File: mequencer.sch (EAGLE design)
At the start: 58 parts, among them IC1 NE555D, IC10 LF353D, IC11 NE555D, IC12 NE555D, IC2 4163D, IC3 74HC85D, IC4 4051D, IC5 4051D, IC6 74HCT04D, IC7 4051D, IC8 4051D, IC9 LF353D

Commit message: 55555555555555555
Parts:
- added C3, C4: 1uF, SparkFun-Capacitors:CAP0603-CAP
- added R22: 1k, SparkFun-Resistors:RESISTOR0603
- added R23: TRIMPOT-2, SparkFun-Electromechanical:TRIMPOT-2
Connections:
- new net N$16: IC11.DIS, R22.2
- new net N$17: IC12.DIS, R23.CW
- new net N$18: C3.2, IC11.TRE
- new net N$20: IC11.TRI, IC6C.O
- new net N$21: C4.2, IC12.TRE
- new net N$23: IC11.OUT, IC12.TRI
- net 5V: now also IC11./RES, IC11.VCC+, IC12./RES, IC12.VCC+, R22.1, R23.WIPER
- net CLOCK: now also IC6C.I
- net GND: now also C3.1, C4.1, IC11.GND
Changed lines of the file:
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@@
 <part name="IC11" library="SparkFun-AnalogIC" deviceset="NE555" device="D"/>
 <part name="IC12" library="SparkFun-AnalogIC" deviceset="NE555" device="D"/>
+<part name="R22" library="SparkFun-Resistors" deviceset="RESISTOR" device="0603" value="1k"/>
+<part name="SUPPLY8" library="SparkFun-Aesthetics" deviceset="5V" device=""/>
+<part name="GND11" library="SparkFun-Aesthetics" deviceset="GND" device=""/>
+<part name="C3" library="SparkFun-Capacitors" deviceset="CAP" device="0603-CAP" value="1uF"/>
+<part name="GND12" library="SparkFun-Aesthetics" deviceset="GND" device=""/>
+<part name="C4" library="SparkFun-Capacitors" deviceset="CAP" device="0603-CAP" value="1uF"/>
+<part name="SUPPLY9" library="SparkFun-Aesthetics" deviceset="5V" device=""/>
+<part name="R23" library="SparkFun-Electromechanical" deviceset="TRIMPOT" device="-2"/>
 </parts>
 <sheets>
@@
 <instance part="IC11" gate="G$1" x="40.64" y="17.78"/>
 <instance part="IC12" gate="G$1" x="73.66" y="17.78"/>
+<instance part="R22" gate="G$1" x="25.4" y="17.78"/>
+<instance part="SUPPLY8" gate="G$1" x="22.86" y="30.48"/>
+<instance part="GND11" gate="1" x="22.86" y="2.54"/>
+<instance part="C3" gate="G$1" x="5.08" y="12.7" rot="R180"/>
+<instance part="IC6" gate="C" x="20.32" y="12.7"/>
+<instance part="GND12" gate="1" x="60.96" y="2.54"/>
+<instance part="C4" gate="G$1" x="58.42" y="25.4" rot="R180"/>
+<instance part="SUPPLY9" gate="G$1" x="71.12" y="30.48"/>
+<instance part="R23" gate="R?" x="53.34" y="30.48" rot="R270"/>
 </instances>
 <busses>
@@
 <wire x1="30.48" y1="86.36" x2="33.02" y2="86.36" width="0.1524" layer="91"/>
 </segment>
+<segment>
+<pinref part="SUPPLY8" gate="G$1" pin="5V"/>
+<wire x1="22.86" y1="30.48" x2="50.8" y2="30.48" width="0.1524" layer="91"/>
+<pinref part="R22" gate="G$1" pin="1"/>
+<wire x1="20.32" y1="17.78" x2="20.32" y2="30.48" width="0.1524" layer="91"/>
+<wire x1="20.32" y1="30.48" x2="22.86" y2="30.48" width="0.1524" layer="91"/>
+<junction x="22.86" y="30.48"/>
+<pinref part="IC11" gate="G$1" pin="/RES"/>
+<pinref part="IC11" gate="G$1" pin="VCC+"/>
+<wire x1="50.8" y1="22.86" x2="50.8" y2="25.4" width="0.1524" layer="91"/>
+<wire x1="50.8" y1="25.4" x2="50.8" y2="30.48" width="0.1524" layer="91"/>
+<junction x="50.8" y="25.4"/>
+</segment>
+<segment>
+<pinref part="R23" gate="R?" pin="WIPER"/>
+<pinref part="SUPPLY9" gate="G$1" pin="5V"/>
+<wire x1="58.42" y1="30.48" x2="71.12" y2="30.48" width="0.1524" layer="91"/>
+<pinref part="IC12" gate="G$1" pin="/RES"/>
+<pinref part="IC12" gate="G$1" pin="VCC+"/>
+<wire x1="83.82" y1="22.86" x2="83.82" y2="25.4" width="0.1524" layer="91"/>
+<wire x1="83.82" y1="25.4" x2="83.82" y2="30.48" width="0.1524" layer="91"/>
+<junction x="83.82" y="25.4"/>
+<wire x1="83.82" y1="30.48" x2="71.12" y2="30.48" width="0.1524" layer="91"/>
+<junction x="71.12" y="30.48"/>
+</segment>
 </net>
 <net name="N$1" class="0">
@@
 <wire x1="30.48" y1="63.5" x2="30.48" y2="60.96" width="0.1524" layer="91"/>
 </segment>
+<segment>
+<pinref part="IC11" gate="G$1" pin="GND"/>
+<wire x1="50.8" y1="10.16" x2="50.8" y2="5.08" width="0.1524" layer="91"/>
+<pinref part="GND11" gate="1" pin="GND"/>
+<wire x1="50.8" y1="5.08" x2="22.86" y2="5.08" width="0.1524" layer="91"/>
+<junction x="22.86" y="5.08"/>
+<pinref part="C3" gate="G$1" pin="1"/>
+<wire x1="22.86" y1="5.08" x2="5.08" y2="5.08" width="0.1524" layer="91"/>
+<wire x1="5.08" y1="5.08" x2="5.08" y2="7.62" width="0.1524" layer="91"/>
+</segment>
+<segment>
+<pinref part="C4" gate="G$1" pin="1"/>
+<wire x1="58.42" y1="20.32" x2="58.42" y2="5.08" width="0.1524" layer="91"/>
+<pinref part="GND12" gate="1" pin="GND"/>
+<wire x1="58.42" y1="5.08" x2="60.96" y2="5.08" width="0.1524" layer="91"/>
+</segment>
 </net>
 <net name="N$2" class="0">
@@
 <wire x1="17.78" y1="99.06" x2="2.54" y2="99.06" width="0.1524" layer="91"/>
 <label x="2.54" y="99.06" size="1.778" layer="95"/>
+</segment>
+<segment>
+<pinref part="IC6" gate="C" pin="I"/>
+<wire x1="10.16" y1="12.7" x2="7.62" y2="12.7" width="0.1524" layer="91"/>
+<label x="7.62" y="12.7" size="1.778" layer="95"/>
 </segment>
 </net>
@@
 </segment>
 </net>
+<net name="N$16" class="0">
+<segment>
+<pinref part="IC11" gate="G$1" pin="DIS"/>
+<pinref part="R22" gate="G$1" pin="2"/>
+</segment>
+</net>
+<net name="N$18" class="0">
+<segment>
+<pinref part="IC11" gate="G$1" pin="TRE"/>
+<pinref part="C3" gate="G$1" pin="2"/>
+<wire x1="5.08" y1="15.24" x2="5.08" y2="25.4" width="0.1524" layer="91"/>
+<wire x1="5.08" y1="25.4" x2="30.48" y2="25.4" width="0.1524" layer="91"/>
+</segment>
+</net>
+<net name="N$20" class="0">
+<segment>
+<pinref part="IC6" gate="C" pin="O"/>
+<pinref part="IC11" gate="G$1" pin="TRI"/>
+<wire x1="30.48" y1="12.7" x2="30.48" y2="10.16" width="0.1524" layer="91"/>
+</segment>
+</net>
+<net name="N$17" class="0">
+<segment>
+<pinref part="R23" gate="R?" pin="CW"/>
+<wire x1="53.34" y1="25.4" x2="53.34" y2="17.78" width="0.1524" layer="91"/>
+<pinref part="IC12" gate="G$1" pin="DIS"/>
+<wire x1="53.34" y1="17.78" x2="63.5" y2="17.78" width="0.1524" layer="91"/>
+</segment>
+</net>
+<net name="N$21" class="0">
+<segment>
+<pinref part="C4" gate="G$1" pin="2"/>
+<pinref part="IC12" gate="G$1" pin="TRE"/>
+<wire x1="58.42" y1="27.94" x2="63.5" y2="27.94" width="0.1524" layer="91"/>
+<wire x1="63.5" y1="27.94" x2="63.5" y2="25.4" width="0.1524" layer="91"/>
+</segment>
+</net>
+<net name="N$23" class="0">
+<segment>
+<pinref part="IC11" gate="G$1" pin="OUT"/>
+<wire x1="50.8" y1="17.78" x2="50.8" y2="15.24" width="0.1524" layer="91"/>
+<wire x1="50.8" y1="15.24" x2="53.34" y2="15.24" width="0.1524" layer="91"/>
+<wire x1="53.34" y1="15.24" x2="53.34" y2="10.16" width="0.1524" layer="91"/>
+<pinref part="IC12" gate="G$1" pin="TRI"/>
+<wire x1="53.34" y1="10.16" x2="63.5" y2="10.16" width="0.1524" layer="91"/>
+</segment>
+</net>

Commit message: Board1 headers and power and stuff. schematic done?
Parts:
- removed LED1, LED10, LED11, LED12, LED13, LED14, LED15, LED16, LED2, LED3, LED4, LED5, LED6, LED7, LED8, LED9: (no value), SparkFun-LED:LED0603
- removed R2, R23: TRIMPOT-2, SparkFun-Electromechanical:TRIMPOT-2
- removed R3, R4: (no value), SparkFun-Resistors:RESISTOR0603
- removed S1: SWITCH-MOMENTARY-2-SMD-1101NE, SparkFun-Electromechanical:SWITCH-MOMENTARY-2-SMD-1101NE
- added C10, C11, C12, C13, C14, C15, C16, C17, C18, C19, C20, C21, C22, C23, C24, C25, C7, C8, C9: .1uF, SparkFun-Capacitors:CAP0603-CAP
- added C5: 1uF, SparkFun-Capacitors:CAP0603-CAP
- added C6: 10uF, SparkFun-Capacitors:CAP0603-CAP
- added FRAME2: FRAME-LETTER, SparkFun-Aesthetics:FRAME-LETTER
- added JP1: M02LOCK_LONGPADS, SparkFun-Connectors:M02LOCK_LONGPADS
- added JP2, JP3: M20, SparkFun-Connectors:M20
- added R24: 100k, SparkFun-Resistors:RESISTOR0603
- added R25: 4k, SparkFun-Resistors:RESISTOR0603
- added U$5: AUDIO-JACKERTHENVAR, erthenvar:AUDIO-JACKERTHENVAR
- added U$6: LM3480IM4, SparkFun-PowerIC:LM3480IM4
- added U1: 74LVC1G08SE-7, SparkFun-DigitalIC:7408SE
- U$1: value SWITCH-SPST-2TV -> M04X2; device SparkFun-Electromechanical:SWITCH-SPST-2TV -> SparkFun-Connectors:M04X2
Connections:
- removed net N$17: IC12.DIS, R23.CW
- removed net N$3: R1.1, R2.CW, R2.WIPER
- removed net N$4: R2.CCW, R3.1
- removed net N$5: U$1.O, U$2.NORM
- removed net N$6: IC1.OUT, U$1.P
- new net CANNEL3: JP2.4
- new net CLOCK_SPEED: JP2.17, R1.1
- new net CV: IC10A.-IN
- new net N$22: IC10A.OUT, U1.B
- new net N$24: IC10A.+IN, R24.1, R25.2
- new net N$25: U1.A
- new net N$26: U1.Y
- new net N$27: C5.2, JP1.2, U$6.IN
- new net N$29: JP3.19
- new net NOTE_LENGTH: IC12.DIS, JP3.18
- new net PAUSE_IN: IC1.OUT, JP2.18
- new net PAUSE_OUT: JP2.19, U$2.NORM
- net 5V: now also C10.2, C11.2, C13.2, C14.2, C15.2, C16.2, C17.2, C18.2, C19.2, C20.2, C21.2, C22.2, C23.2, C24.2, C25.2, C6.2, C7.2, C8.2, C9.2, JP3.20, R25.1, U$6.OUT, U1.VCC; no longer R23.WIPER, R3.2
- net CHANNEL10: now also JP2.11
- net CHANNEL11: now also JP2.12
- net CHANNEL12: now also JP2.13
- net CHANNEL13: now also JP2.14
- net CHANNEL14: now also JP2.15
- net CHANNEL15: now also JP2.16
- net CHANNEL2: now also JP2.3
- net CHANNEL4: now also JP2.5
- net CHANNEL5: now also JP2.6
- net CHANNEL6: now also JP2.7
- net CHANNEL8: now also JP2.9
- net CHANNEL9: now also JP2.10
- net GND: now also C5.1, C6.1, IC10P.V-, IC3P.GND, IC4P.GND, IC4P.VEE, IC5P.GND, IC5P.VEE, IC6P.GND, IC7P.GND, IC7P.VEE, IC8P.GND, IC8P.VEE, IC9P.V-, JP1.1, JP2.20, R24.2, U$5.RING, U$6.GND, U1.GND; no longer LED1.C, LED10.C, LED11.C, LED12.C, LED13.C, LED14.C, LED15.C, LED16.C, LED2.C, LED3.C, LED4.C, LED5.C, LED6.C, LED7.C, LED8.C, LED9.C, R4.1
- net LED0: no longer LED1.A
- net LED1: now also JP3.2; no longer LED2.A
- net LED10: now also JP3.11; no longer LED11.A
- net LED11: now also JP3.12; no longer LED12.A
- net LED12: now also JP3.13; no longer LED13.A
- net LED13: now also JP3.14; no longer LED14.A
- net LED14: now also JP3.15; no longer LED15.A
- net LED15: now also JP3.16; no longer LED16.A
- net LED2: now also JP3.3; no longer LED3.A
- net LED3: now also JP3.4; no longer LED4.A
- net LED4: now also JP3.5; no longer LED5.A
- net LED5: now also JP3.6; no longer LED6.A
- net LED6: now also JP3.7; no longer LED7.A
- net LED7: now also JP3.8; no longer LED8.A
- net LED8: now also JP3.9; no longer LED9.A
- net LED9: now also JP3.10; no longer LED10.A
- net LOAD: no longer S1.2
- net LOAD0: now also U$1.2
- net LOAD1: now also U$1.4
- net LOAD2: now also U$1.6
- net LOAD3: now also U$1.8
- net N$7: now also C10.1, C11.1, C12.1, C13.1, C14.1, C15.1, C16.1, C17.1, C18.1, C19.1, C20.1, C21.1, C22.1, C23.1, C24.1, C25.1, C7.1, C8.1, C9.1, IC10P.V+, IC2P.VDD, IC3P.VCC, IC4P.VCC, IC5P.VCC, IC6P.VCC, IC7P.VCC, IC8P.VCC, IC9P.V+; no longer R4.2, S1.1
- net RESET0: now also U$1.1
- net RESET1: now also U$1.3
- net RESET3: now also U$1.7

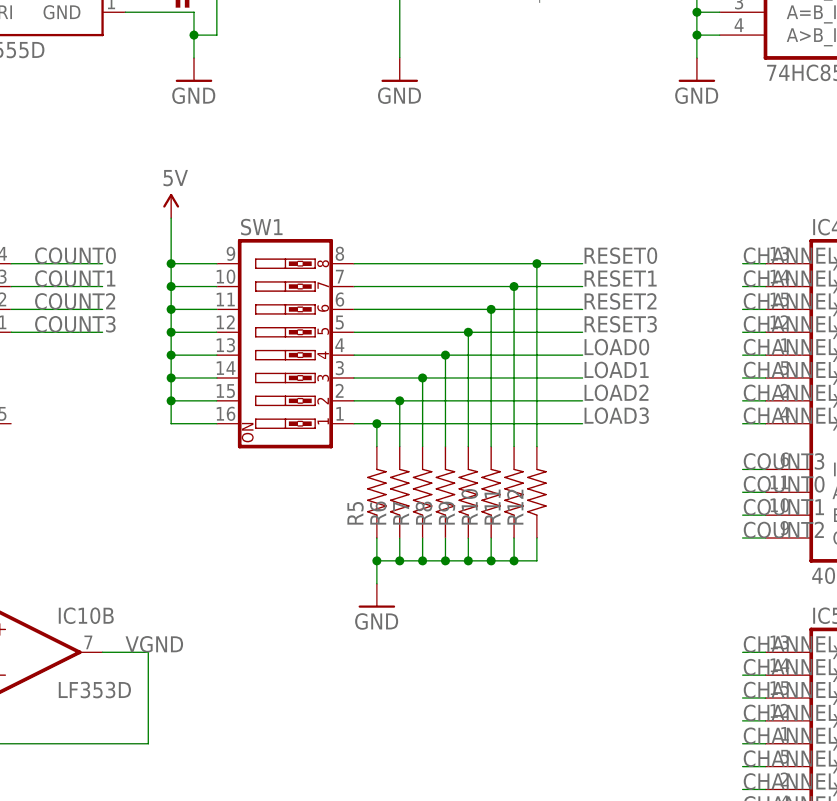
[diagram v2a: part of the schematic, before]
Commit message: Added knobby expansion board
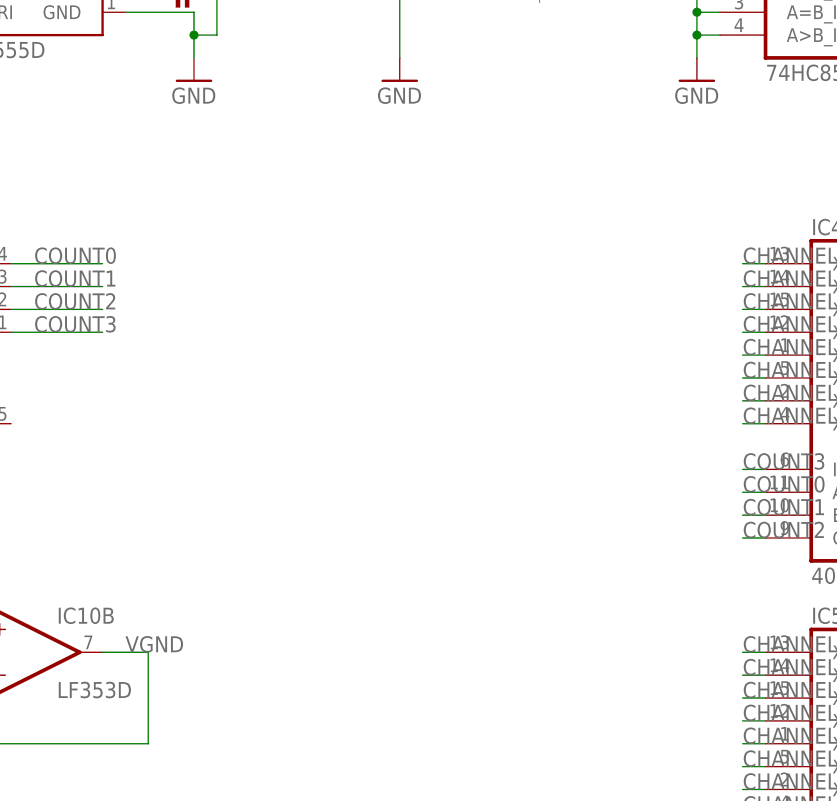
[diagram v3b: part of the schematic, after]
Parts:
- removed R10, R11, R12, R5, R6, R7, R8, R9: (no value), SparkFun-Resistors:RESISTOR0603
- removed SW1: (no value), SparkFun-Electromechanical:SW_DIP-8
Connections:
- net 5V: no longer SW1.10, SW1.11, SW1.12, SW1.13, SW1.14, SW1.15, SW1.16, SW1.9
- net GND: no longer R10.1, R11.1, R12.1, R5.1, R6.1, R7.1, R8.1, R9.1
- net LOAD0: no longer R8.2, SW1.4
- net LOAD1: no longer R7.2, SW1.3
- net LOAD2: no longer R6.2, SW1.2
- net LOAD3: no longer R5.2, SW1.1
- net RESET0: no longer R12.2, SW1.8
- net RESET1: no longer R11.2, SW1.7
- net RESET2: no longer R10.2, SW1.6
- net RESET3: no longer R9.2, SW1.5

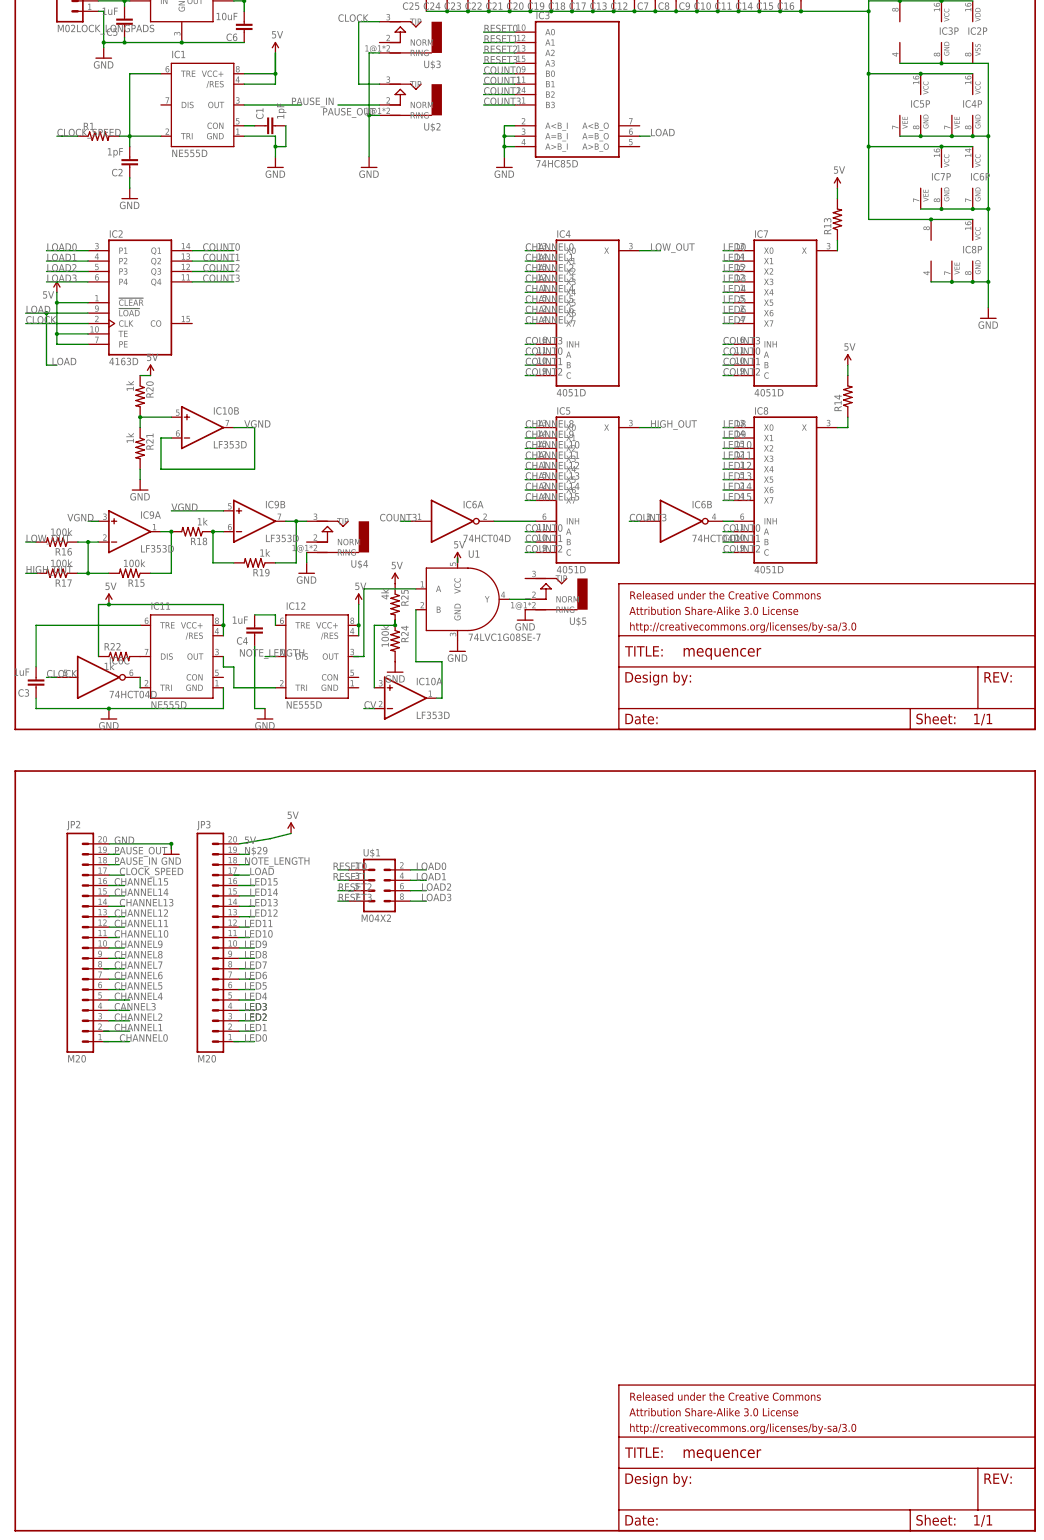
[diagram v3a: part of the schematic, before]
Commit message: Added LEDS to knobby board
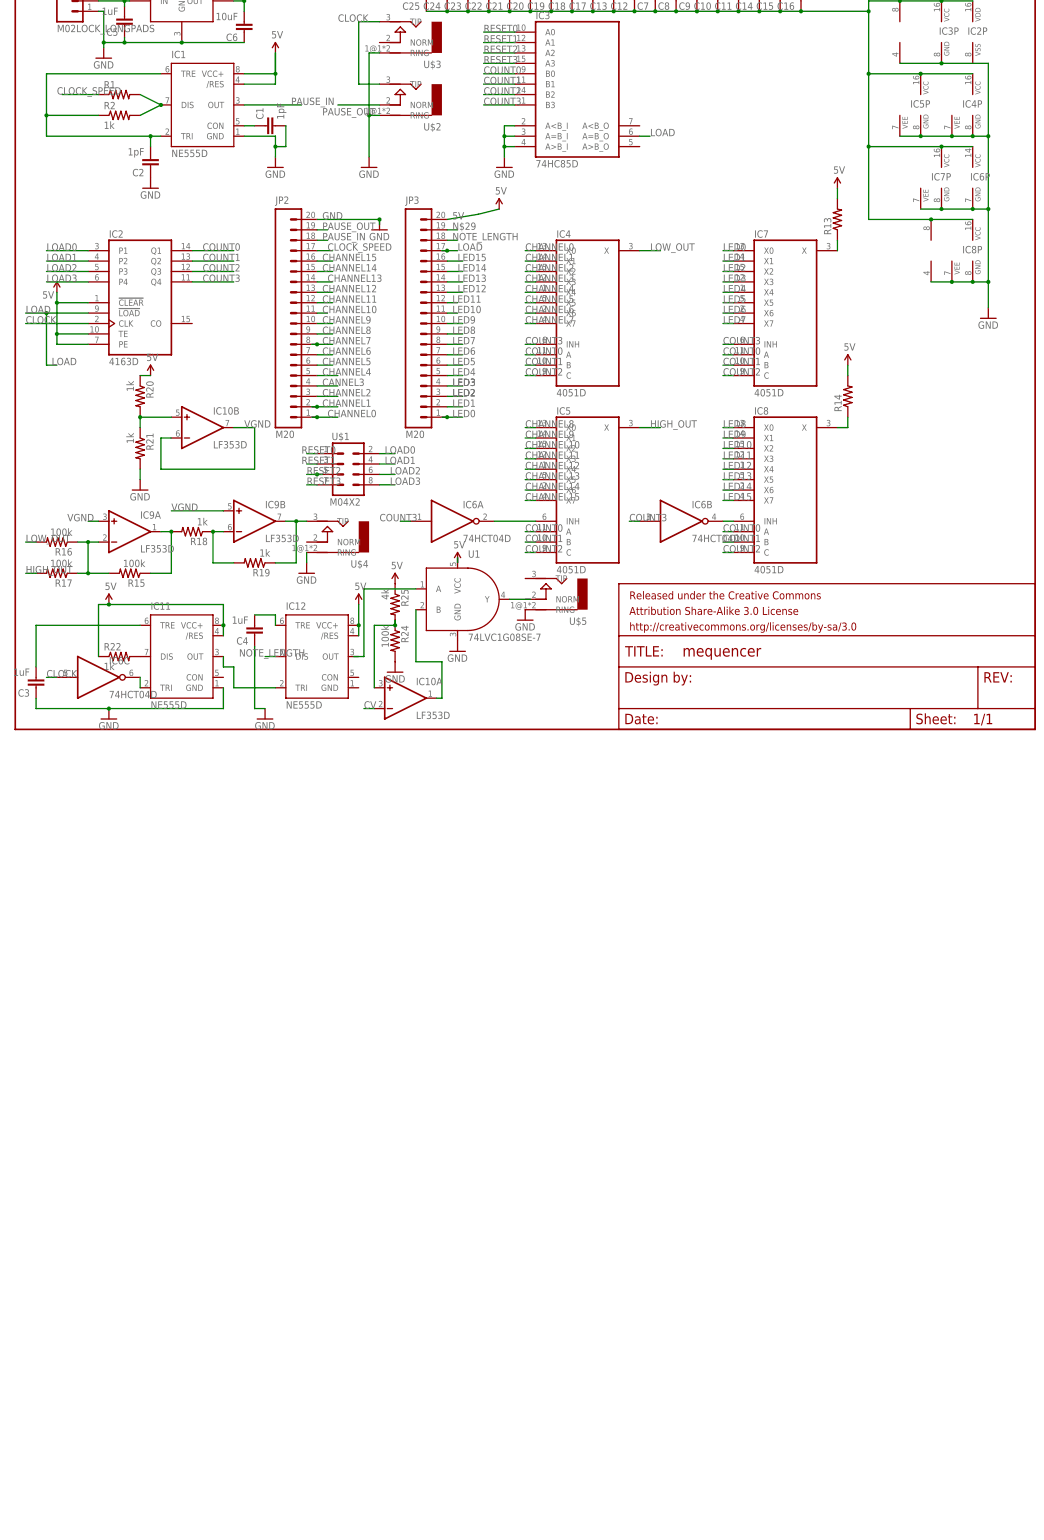
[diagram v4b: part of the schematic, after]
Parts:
- removed FRAME2: FRAME-LETTER, SparkFun-Aesthetics:FRAME-LETTER
- added R2: 1k, SparkFun-Resistors:RESISTOR0603
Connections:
- removed net N$1: C2.2, IC1.TRE, IC1.TRI, R1.2
- new net N$3: IC1.DIS, R1.2, R2.2
- new net N$4: C2.2, IC1.TRE, IC1.TRI, R2.1
- net CHANNEL0: now also JP2.1
- net CHANNEL1: now also JP2.2
- net CHANNEL7: now also JP2.8
- net LED0: now also JP3.1
- net LOAD: now also JP3.17
- net RESET2: now also U$1.5
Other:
- moved on the sheet: C2, JP2, JP3, R1, U$1
